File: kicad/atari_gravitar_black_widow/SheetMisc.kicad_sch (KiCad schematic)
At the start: 5 parts, among them J17 cat_box_con, J19 J19, J20 J20

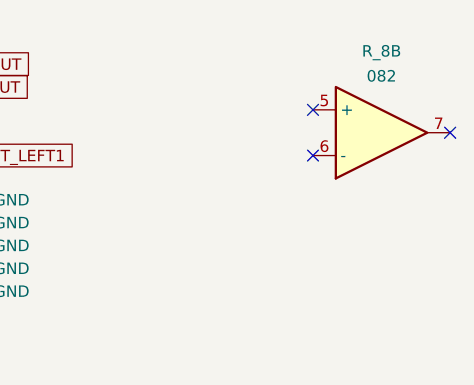
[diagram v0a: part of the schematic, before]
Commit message: Removed more warnings - 25 warnings remain
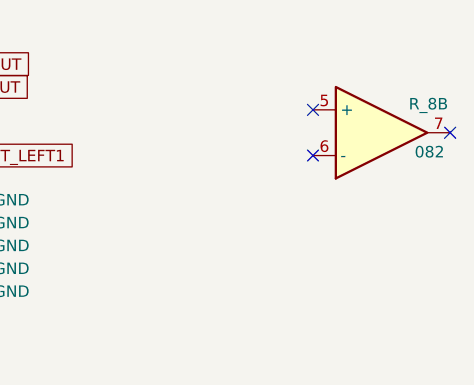
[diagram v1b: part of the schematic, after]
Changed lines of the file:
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@@
     (pin "1")
+  )
+  (symbol (lib_id "atari_grav_bw:082") (at 262.89 36.195 0) (unit 2)
+    (in_bom yes) (on_board yes)
+    (property "Reference" "R_8" (id 0) (at 268.097 33.02 0))
+    (property "Value" "082" (id 1) (at 268.224 38.354 0))
+    (property "Footprint" "" (id 2) (at 262.89 36.195 0)
+      (effects (font (size 1.27 1.27)) hide)
+    )
+    (property "Datasheet" "" (id 3) (at 262.89 36.195 0)
+      (effects (font (size 1.27 1.27)) hide)
+    )
+    (pin "5")
+    (pin "6")
+    (pin "7")
   )
   (symbol (lib_id "power:PWR_FLAG") (at 72.39 94.996 0) (unit 1)
@@
     (pin "2")
   )
-  (symbol (lib_name "082_1") (lib_id "atari_grav_bw:082") (at 262.89 36.195 0) (unit 2)
-    (in_bom yes) (on_board yes) (fields_autoplaced)
-    (property "Reference" "R_8" (id 0) (at 262.89 27.1485 0))
-    (property "Value" "082" (id 1) (at 262.89 29.9236 0))
-    (property "Footprint" "" (id 2) (at 262.89 36.195 0)
-      (effects (font (size 1.27 1.27)) hide)
-    )
-    (property "Datasheet" "" (id 3) (at 262.89 36.195 0)
-      (effects (font (size 1.27 1.27)) hide)
-    )
-    (pin "5")
-    (pin "6")
-    (pin "7")
-  )
   (symbol (lib_id "power:+24V") (at 69.088 94.996 90) (unit 1)

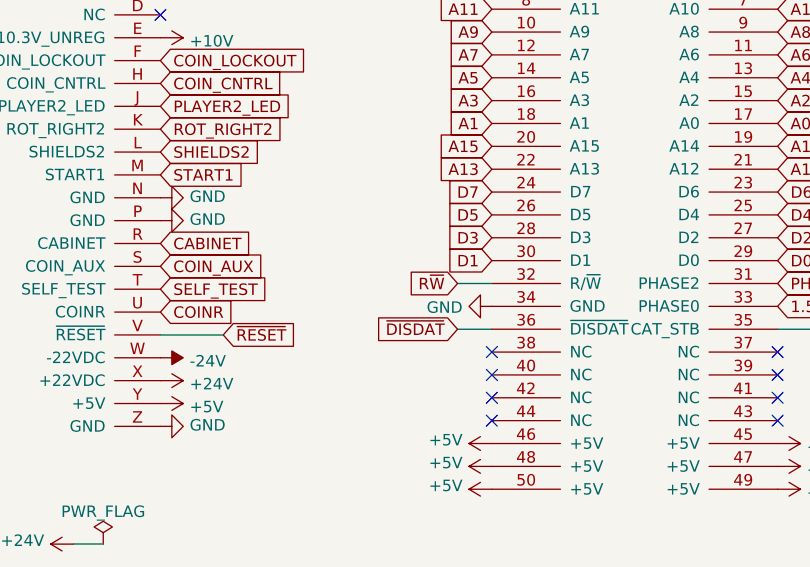
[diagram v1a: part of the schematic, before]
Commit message: 20 warnings left kicad 6.0
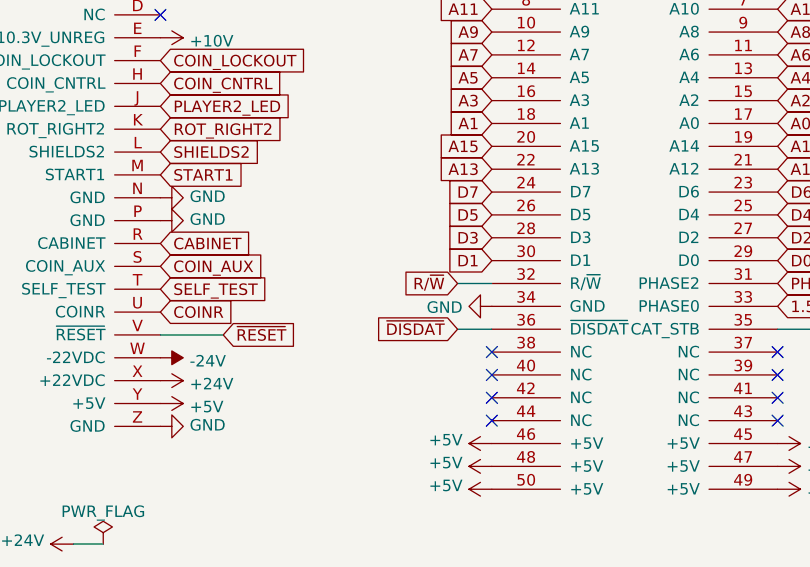
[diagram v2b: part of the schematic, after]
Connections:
- net R~{W} renamed R/~{W}
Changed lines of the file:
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@@
     )
   )
-  (global_label "R~{W}" (shape input) (at 111.76 66.04 180) (fields_autoplaced)
+  (global_label "R{slash}~{W}" (shape input) (at 111.76 66.04 180) (fields_autoplaced)
     (effects (font (size 1.27 1.27)) (justify right))
-    (property "Intersheet References" "${INTERSHEET_REFS}" (id 0) (at 0 0 0)
-      (effects (font (size 1.27 1.27)) hide)
+    (property "Intersheet References" "${INTERSHEET_REFS}" (id 0) (at 105.3839 65.9606 0)
+      (effects (font (size 1.27 1.27)) (justify right) hide)
     )
   )

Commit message: placements
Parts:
- R_8: footprint (none) -> Star_Wars_Vector_PCB:DIP8
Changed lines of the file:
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@@
     (property "Reference" "R_8" (id 0) (at 268.097 33.02 0))
     (property "Value" "082" (id 1) (at 268.224 38.354 0))
-    (property "Footprint" "" (id 2) (at 262.89 36.195 0)
+    (property "Footprint" "Star_Wars_Vector_PCB:DIP8" (id 2) (at 262.89 36.195 0)
       (effects (font (size 1.27 1.27)) hide)
     )

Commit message: TEST POINTS PLACED
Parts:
- TPCAT_STROBE1: footprint (none) -> quantum_arcade_pcb:TP
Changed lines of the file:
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@@
       (effects (font (size 1.524 1.524)) hide)
     )
-    (property "Footprint" "" (id 2) (at 164.465 67.31 0)
+    (property "Footprint" "quantum_arcade_pcb:TP" (id 2) (at 164.465 67.31 0)
       (effects (font (size 1.524 1.524)) hide)
     )

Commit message: Worked on traces and components
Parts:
- J17: footprint (none) -> Asteroids:J21
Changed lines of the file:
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@@
     (property "Reference" "J17" (id 0) (at 137.16 24.765 0))
     (property "Value" "cat_box_con" (id 1) (at 122.555 24.765 0))
-    (property "Footprint" "" (id 2) (at 132.08 10.16 0)
+    (property "Footprint" "Asteroids:J21" (id 2) (at 132.08 10.16 0)
       (effects (font (size 1.27 1.27)) hide)
     )

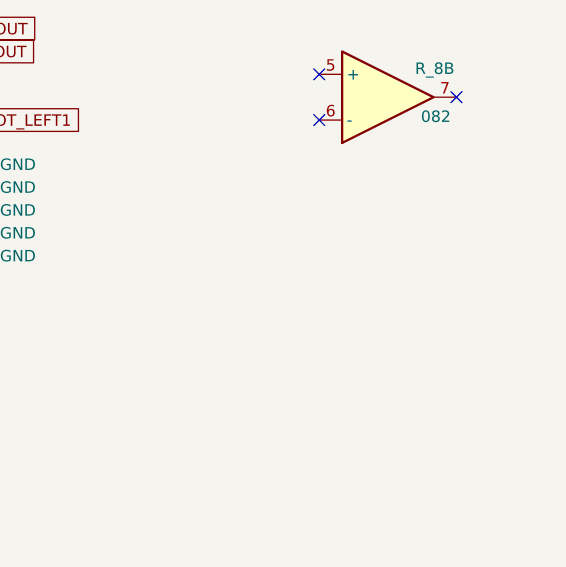
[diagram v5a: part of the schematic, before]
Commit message: Added traces and bottom image
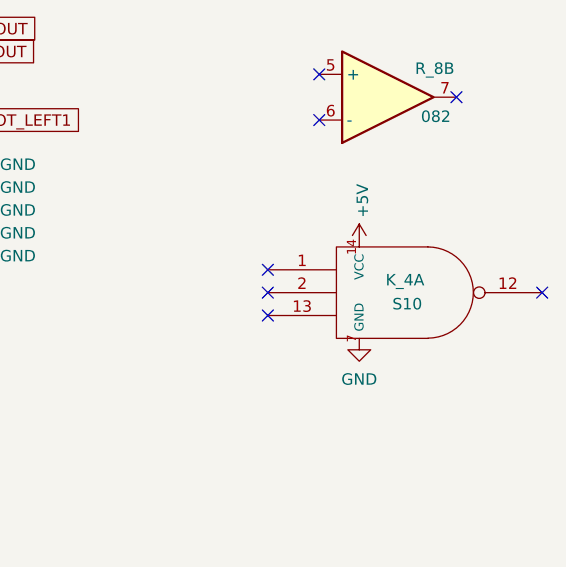
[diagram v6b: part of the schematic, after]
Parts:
- added K_4: S10, Star_Wars_Vector_PCB:DIP14, symbol atari_grav_bw:LS10
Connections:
- net +5V: now also K_4.14 (VCC)
- net GND: now also K_4.7 (GND)
- no-connect marks 22 -> 26
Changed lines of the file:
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@@
   (no_connect (at 255.27 38.735))
   (no_connect (at 38.1 76.835))
+  (no_connect (at 249.555 55.372))
+  (no_connect (at 249.555 57.912))
+  (no_connect (at 249.555 60.452))
+  (no_connect (at 280.035 57.912))
   (no_connect (at 38.1 64.135))
   (no_connect (at 147.32 78.74))
@@
     (pin "1")
   )
+  (symbol (lib_id "power:GND") (at 259.715 62.992 0) (unit 1)
+    (in_bom yes) (on_board yes) (fields_autoplaced)
+    (property "Reference" "#PWR0540" (id 0) (at 259.715 69.342 0)
+      (effects (font (size 1.27 1.27)) hide)
+    )
+    (property "Value" "GND" (id 1) (at 259.715 67.5545 0))
+    (property "Footprint" "" (id 2) (at 259.715 62.992 0)
+      (effects (font (size 1.27 1.27)) hide)
+    )
+    (property "Datasheet" "" (id 3) (at 259.715 62.992 0)
+      (effects (font (size 1.27 1.27)) hide)
+    )
+    (pin "1")
+  )
   (symbol (lib_id "power:PWR_FLAG") (at 44.45 95.758 0) (unit 1)
     (in_bom yes) (on_board yes) (fields_autoplaced)
@@
     (pin "1")
   )
+  (symbol (lib_id "atari_grav_bw:LS10") (at 264.795 57.912 0) (unit 1)
+    (in_bom yes) (on_board yes)
+    (property "Reference" "K_4" (id 0) (at 264.795 56.515 0))
+    (property "Value" "S10" (id 1) (at 265.049 59.182 0))
+    (property "Footprint" "Star_Wars_Vector_PCB:DIP14" (id 2) (at 264.795 57.912 0)
+      (effects (font (size 1.27 1.27)) hide)
+    )
+    (property "Datasheet" "" (id 3) (at 264.795 57.912 0)
+      (effects (font (size 1.27 1.27)) hide)
+    )
+    (pin "14")
+    (pin "7")
+    (pin "1")
+    (pin "12")
+    (pin "13")
+    (pin "2")
+  )
   (symbol (lib_id "power:PWR_FLAG") (at 48.26 104.394 0) (unit 1)
     (in_bom yes) (on_board yes) (fields_autoplaced)
@@
       (effects (font (size 1.27 1.27)) hide)
     )
+    (pin "1")
+  )
+  (symbol (lib_id "power:+5V") (at 259.715 52.832 0) (unit 1)
+    (in_bom yes) (on_board yes)
+    (property "Reference" "#PWR0235" (id 0) (at 259.715 56.642 0)
+      (effects (font (size 1.27 1.27)) hide)
+    )
+    (property "Value" "+5V" (id 1) (at 260.096 49.5808 90)
+      (effects (font (size 1.27 1.27)) (justify left))
+    )
+    (property "Footprint" "" (id 2) (at 259.715 52.832 0)
+      (effects (font (size 1.27 1.27)) hide)
+    )
+    (property "Datasheet" "" (id 3) (at 259.715 52.832 0)
+      (effects (font (size 1.27 1.27)) hide)
+    )

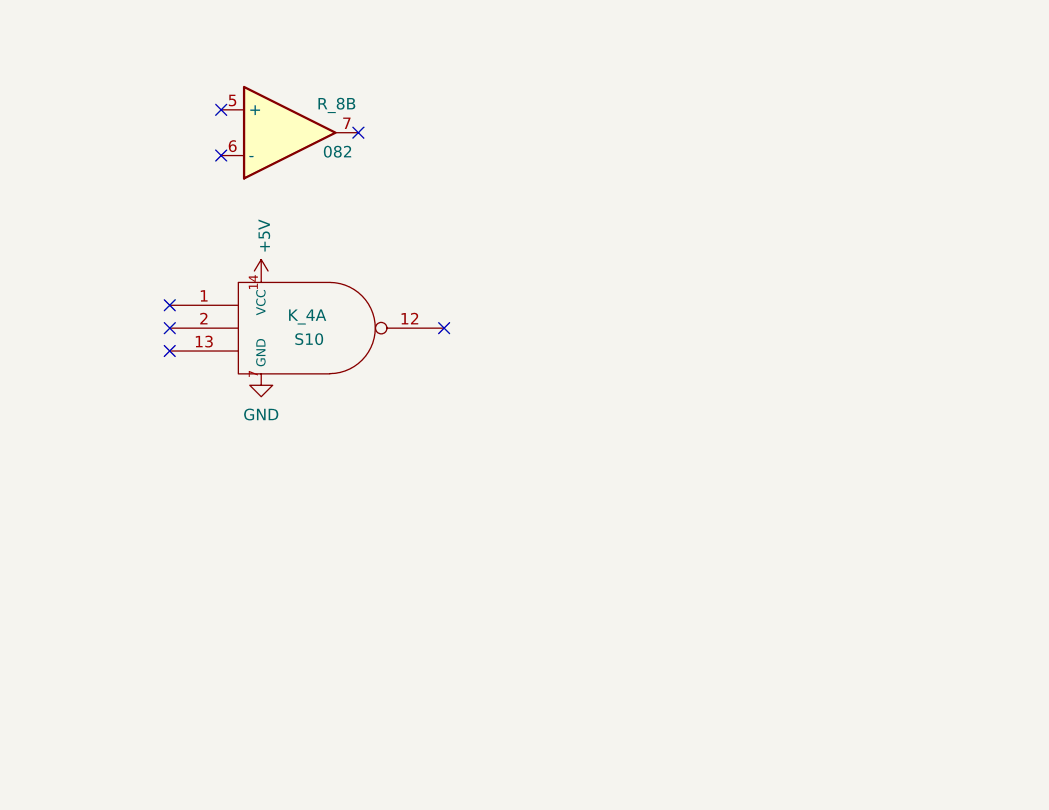
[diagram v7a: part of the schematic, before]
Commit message: Fixed all schematic warnings and fixed the edge cuts
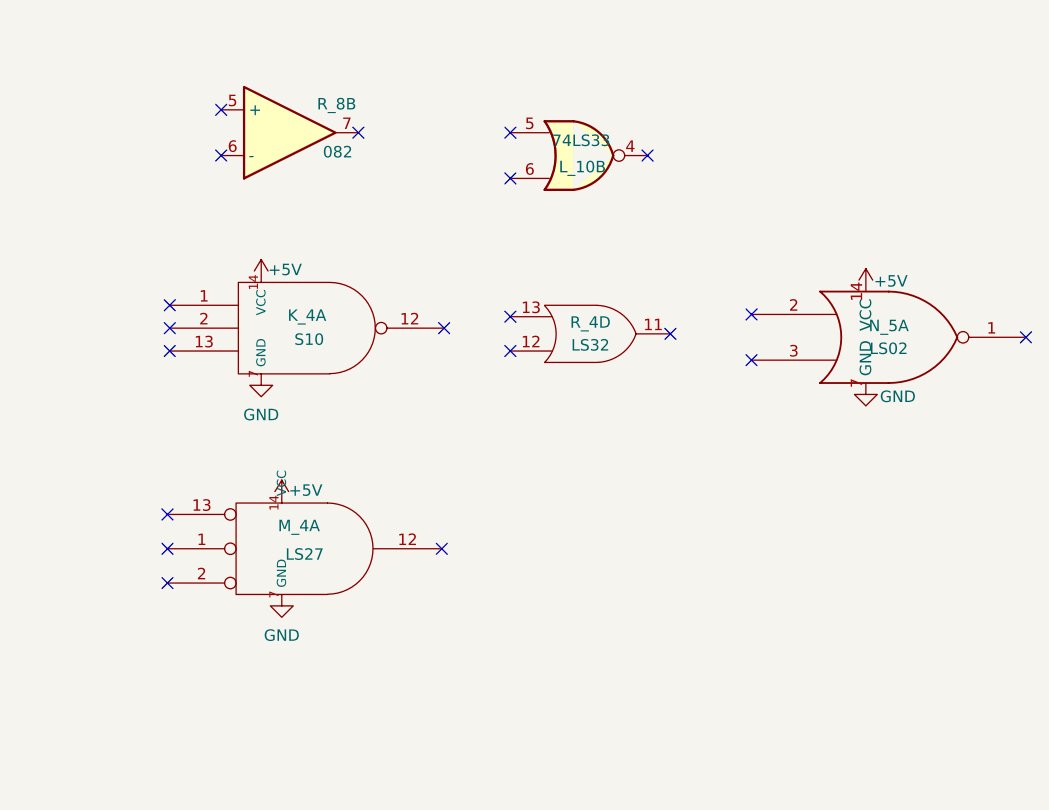
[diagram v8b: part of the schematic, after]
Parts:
- added L_10: 74LS33, Star_Wars_Vector_PCB:DIP14, symbol 74xx:74LS33
- added M_4: LS27, Star_Wars_Vector_PCB:DIP14, symbol atari_grav_bw:LS27A
- added N_5: LS02, Star_Wars_Vector_PCB:DIP14, symbol atari_grav_bw:LS02
- added R_4: LS32, Star_Wars_Vector_PCB:DIP14, symbol atari_grav_bw:LS32
- J19: footprint (none) -> Gravitar:J19
- J20: footprint (none) -> Asteroids:J20
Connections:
- net +5V: now also M_4.14 (VCC), N_5.14 (VCC)
- net GND: now also M_4.7 (GND), N_5.7 (GND)
- no-connect marks 26 -> 39
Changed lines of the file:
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@@
   (no_connect (at 255.27 38.735))
   (no_connect (at 38.1 76.835))
+  (no_connect (at 302.641 38.735))
+  (no_connect (at 287.401 36.195))
+  (no_connect (at 287.401 41.275))
   (no_connect (at 249.555 55.372))
   (no_connect (at 249.555 57.912))
@@
   (no_connect (at 38.1 64.135))
   (no_connect (at 147.32 78.74))
+  (no_connect (at 314.198 61.468))
+  (no_connect (at 344.678 58.928))
+  (no_connect (at 314.198 56.388))
+  (no_connect (at 287.401 60.452))
+  (no_connect (at 287.401 56.642))
+  (no_connect (at 305.181 58.547))
   (no_connect (at 216.535 36.195))
   (no_connect (at 270.51 36.195))
+  (no_connect (at 249.301 78.613))
+  (no_connect (at 249.301 82.423))
+  (no_connect (at 249.301 86.233))
+  (no_connect (at 279.781 82.423))
   (no_connect (at 78.74 33.655))
   (no_connect (at 115.57 73.66))
@@
     (property "Reference" "J20" (id 0) (at 45.72 26.035 0))
     (property "Value" "J20" (id 1) (at 71.12 26.035 0))
-    (property "Footprint" "" (id 2) (at 58.42 51.435 0)
+    (property "Footprint" "Asteroids:J20" (id 2) (at 58.42 51.435 0)
       (effects (font (size 1.27 1.27)) hide)
     )
@@
     (property "Reference" "J19" (id 0) (at 208.915 26.035 0))
     (property "Value" "J19" (id 1) (at 183.515 26.035 0))
-    (property "Footprint" "" (id 2) (at 193.675 38.735 0)
+    (property "Footprint" "Gravitar:J19" (id 2) (at 193.675 38.735 0)
       (effects (font (size 1.27 1.27)) hide)
     )
@@
     (pin "1")
   )
+  (symbol (lib_id "74xx:74LS33") (at 295.021 38.735 0) (unit 2)
+    (in_bom yes) (on_board yes)
+    (property "Reference" "L_10" (id 0) (at 295.402 40.005 0))
+    (property "Value" "74LS33" (id 1) (at 295.275 37.084 0))
+    (property "Footprint" "Star_Wars_Vector_PCB:DIP14" (id 2) (at 295.021 38.735 0)
+      (effects (font (size 1.27 1.27)) hide)
+    )
+    (property "Datasheet" "http://www.ti.com/lit/gpn/sn74LS33" (id 3) (at 295.021 38.735 0)
+      (effects (font (size 1.27 1.27)) hide)
+    )
+    (pin "4")
+    (pin "5")
+    (pin "6")
+  )
   (symbol (lib_id "power:PWR_FLAG") (at 44.45 95.758 0) (unit 1)
     (in_bom yes) (on_board yes) (fields_autoplaced)
@@
     (pin "1")
   )
+  (symbol (lib_id "atari_grav_bw:LS02") (at 329.438 58.928 0) (unit 1)
+    (in_bom yes) (on_board yes)
+    (property "Reference" "N_5" (id 0) (at 329.438 57.658 0))
+    (property "Value" "LS02" (id 1) (at 329.438 60.198 0))
+    (property "Footprint" "Star_Wars_Vector_PCB:DIP14" (id 2) (at 329.438 58.928 0)
+      (effects (font (size 1.27 1.27)) hide)
+    )
+    (property "Datasheet" "" (id 3) (at 329.438 58.928 0)
+      (effects (font (size 1.27 1.27)) hide)
+    )
+    (pin "14")
+    (pin "7")
+    (pin "1")
+    (pin "2")
+    (pin "3")
+  )
   (symbol (lib_id "power:+5V") (at 44.45 104.394 90) (unit 1)
     (in_bom yes) (on_board yes)
@@
     )
     (pin "1")
+  )
+  (symbol (lib_id "atari_grav_bw:LS27A") (at 264.541 82.423 0) (unit 1) (convert 2)
+    (in_bom yes) (on_board yes)
+    (property "Reference" "M_4" (id 0) (at 263.906 79.883 0))
+    (property "Value" "LS27" (id 1) (at 264.541 83.058 0))
+    (property "Footprint" "Star_Wars_Vector_PCB:DIP14" (id 2) (at 264.541 82.423 0)
+      (effects (font (size 1.27 1.27)) hide)
+    )
+    (property "Datasheet" "" (id 3) (at 264.541 82.423 0)
+      (effects (font (size 1.27 1.27)) hide)
+    )
+    (pin "14")
+    (pin "7")
+    (pin "1")
+    (pin "12")
+    (pin "13")
+    (pin "2")
+  )
+  (symbol (lib_id "power:+5V") (at 326.898 53.848 0) (unit 1)
+    (in_bom yes) (on_board yes)
+    (property "Reference" "#PWR0546" (id 0) (at 326.898 57.658 0)
+      (effects (font (size 1.27 1.27)) hide)
+    )
+    (property "Value" "+5V" (id 1) (at 327.787 52.705 0)
+      (effects (font (size 1.27 1.27)) (justify left))
+    )
+    (property "Footprint" "" (id 2) (at 326.898 53.848 0)
+      (effects (font (size 1.27 1.27)) hide)
+    )
+    (property "Datasheet" "" (id 3) (at 326.898 53.848 0)
+      (effects (font (size 1.27 1.27)) hide)
+    )
+    (pin "1")
+  )
+  (symbol (lib_id "atari_grav_bw:LS32") (at 296.291 58.547 0) (mirror x) (unit 4)
+    (in_bom yes) (on_board yes)
+    (property "Reference" "R_4" (id 0) (at 296.291 57.277 0))
+    (property "Value" "LS32" (id 1) (at 296.291 59.817 0))
+    (property "Footprint" "Star_Wars_Vector_PCB:DIP14" (id 2) (at 296.291 58.547 0)
+      (effects (font (size 1.27 1.27)) hide)
+    )
+    (property "Datasheet" "" (id 3) (at 296.291 58.547 0)
+      (effects (font (size 1.27 1.27)) hide)
+    )
+    (pin "11")
+    (pin "12")
+    (pin "13")
   )
   (symbol (lib_id "atari_grav_bw:LS10") (at 264.795 57.912 0) (unit 1)
@@
     (pin "2")
   )
+  (symbol (lib_id "power:GND") (at 326.898 64.008 0) (unit 1)
+    (in_bom yes) (on_board yes)
+    (property "Reference" "#PWR0545" (id 0) (at 326.898 70.358 0)
+      (effects (font (size 1.27 1.27)) hide)
+    )
+    (property "Value" "GND" (id 1) (at 330.454 65.532 0))
+    (property "Footprint" "" (id 2) (at 326.898 64.008 0)
+      (effects (font (size 1.27 1.27)) hide)
+    )
+    (property "Datasheet" "" (id 3) (at 326.898 64.008 0)
+      (effects (font (size 1.27 1.27)) hide)
+    )
+    (pin "1")
+  )
   (symbol (lib_id "power:PWR_FLAG") (at 48.26 104.394 0) (unit 1)
     (in_bom yes) (on_board yes) (fields_autoplaced)
@@
     (pin "1")
   )
+  (symbol (lib_id "power:GND") (at 262.001 87.503 0) (unit 1)
+    (in_bom yes) (on_board yes) (fields_autoplaced)
+    (property "Reference" "#PWR0548" (id 0) (at 262.001 93.853 0)
+      (effects (font (size 1.27 1.27)) hide)
+    )
+    (property "Value" "GND" (id 1) (at 262.001 92.0655 0))
+    (property "Footprint" "" (id 2) (at 262.001 87.503 0)
+      (effects (font (size 1.27 1.27)) hide)
+    )
+    (property "Datasheet" "" (id 3) (at 262.001 87.503 0)
+      (effects (font (size 1.27 1.27)) hide)
+    )
+    (pin "1")
+  )
   (symbol (lib_id "atari_grav_bw:082") (at 262.89 36.195 0) (unit 2)
     (in_bom yes) (on_board yes)
@@
       (effects (font (size 1.27 1.27)) hide)
     )
-    (property "Value" "+5V" (id 1) (at 260.096 49.5808 90)
+    (property "Value" "+5V" (id 1) (at 260.477 51.435 0)
       (effects (font (size 1.27 1.27)) (justify left))
     )
@@
       (effects (font (size 1.27 1.27)) hide)
     )
+    (pin "1")
+  )
+  (symbol (lib_id "power:+5V") (at 262.001 77.343 0) (unit 1)
+    (in_bom yes) (on_board yes)
+    (property "Reference" "#PWR0547" (id 0) (at 262.001 81.153 0)
+      (effects (font (size 1.27 1.27)) hide)
+    )
+    (property "Value" "+5V" (id 1) (at 262.763 75.946 0)
+      (effects (font (size 1.27 1.27)) (justify left))
+    )
+    (property "Footprint" "" (id 2) (at 262.001 77.343 0)
+      (effects (font (size 1.27 1.27)) hide)
+    )
+    (property "Datasheet" "" (id 3) (at 262.001 77.343 0)
+      (effects (font (size 1.27 1.27)) hide)
+    )
